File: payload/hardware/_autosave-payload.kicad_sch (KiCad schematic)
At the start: 4 parts, among them J1 522071585, J2 Conn_01x05, U1 CM4102008, U3 CD74HC4067SM

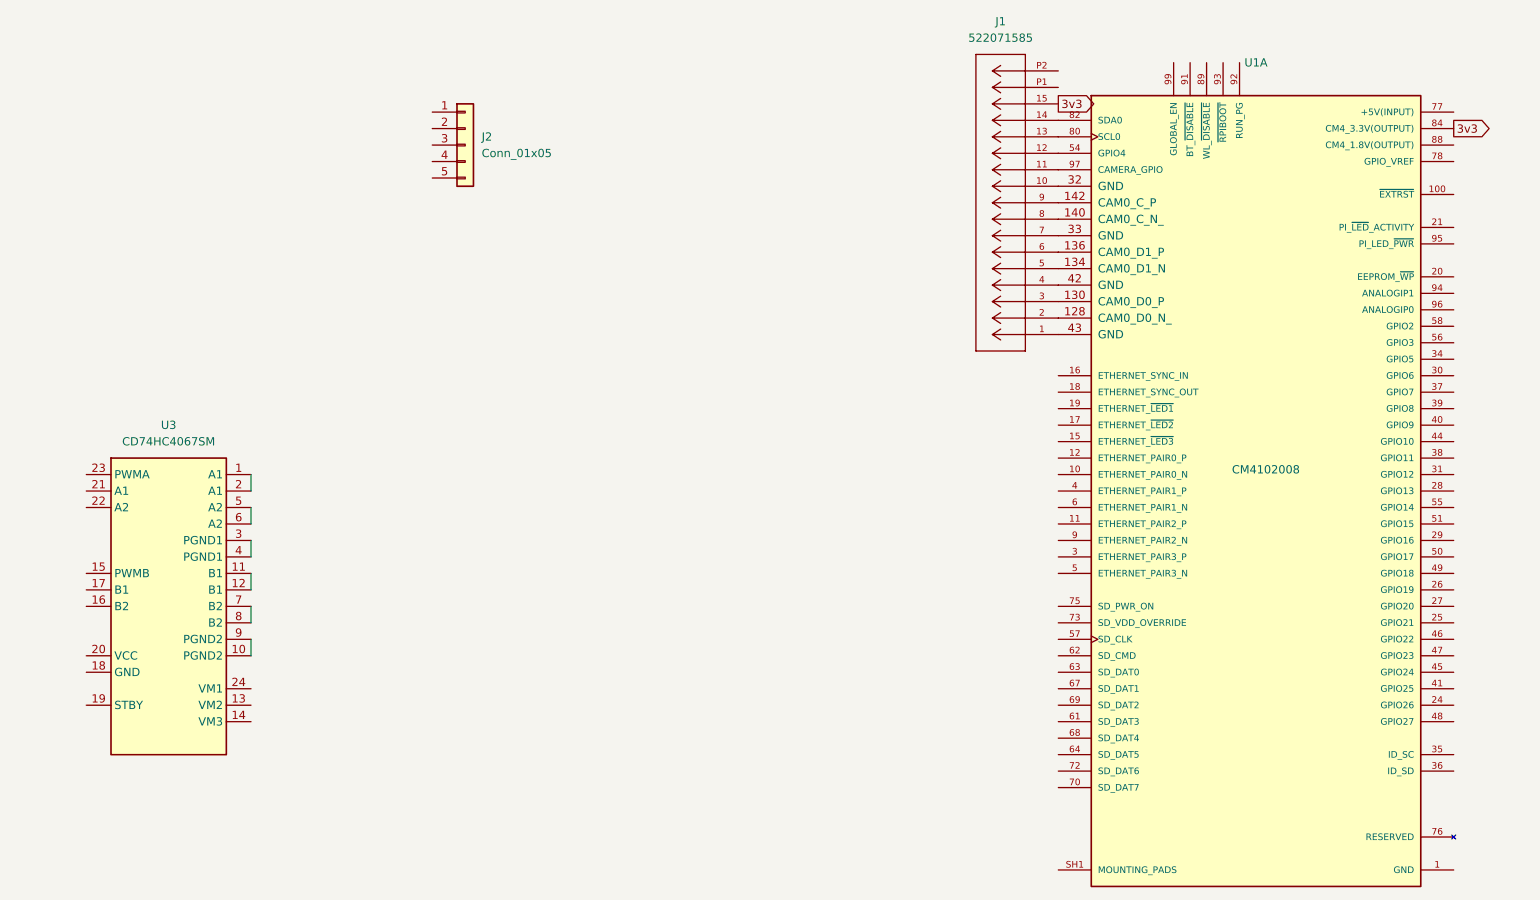
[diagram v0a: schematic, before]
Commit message: added the motordriver to payload schematic
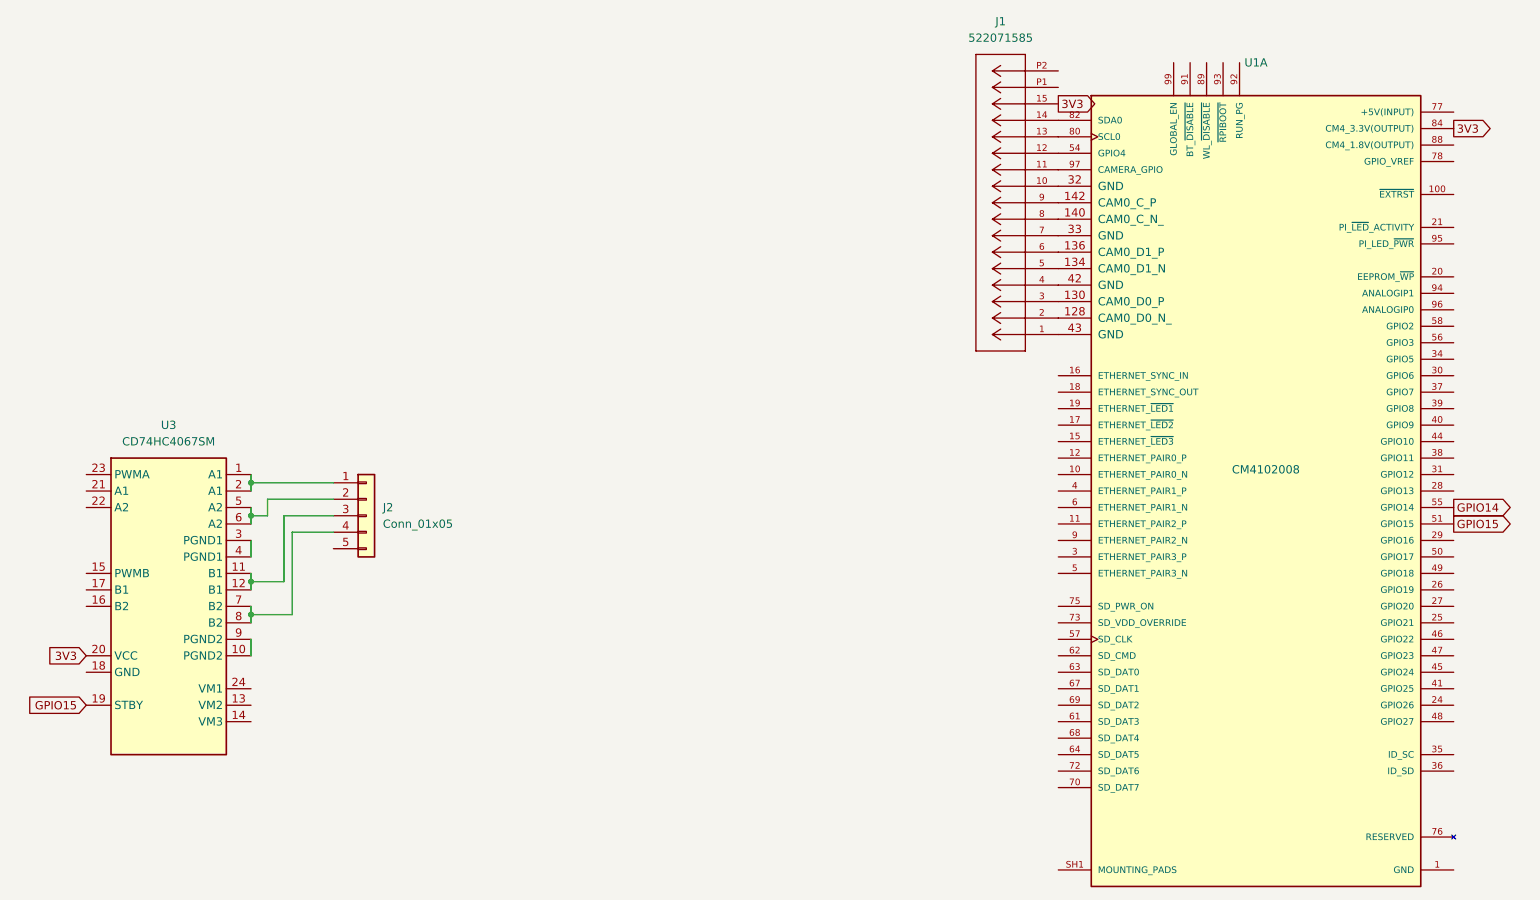
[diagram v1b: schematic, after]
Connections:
- net CM4_3.3V(OUTPUT): now also U3.20 (VCC)
- net at U3.1 (A1), U3.2 (A1): now also J2.1 (Pin_1)
- net at U3.11 (B1), U3.12 (B1): now also J2.3 (Pin_3)
- net GPIO15: now reaches U3.19 (STBY)
- net GPIO15: now also U1.51 (GPIO15)
- net at U3.5 (A2), U3.6 (A2): now also J2.2 (Pin_2)
- net at U3.7 (B2), U3.8 (B2): now also J2.4 (Pin_4)
- net GPIO14: now reaches U1.55 (GPIO14)
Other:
- moved on the sheet: J2
